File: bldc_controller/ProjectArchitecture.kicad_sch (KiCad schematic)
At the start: 0 parts

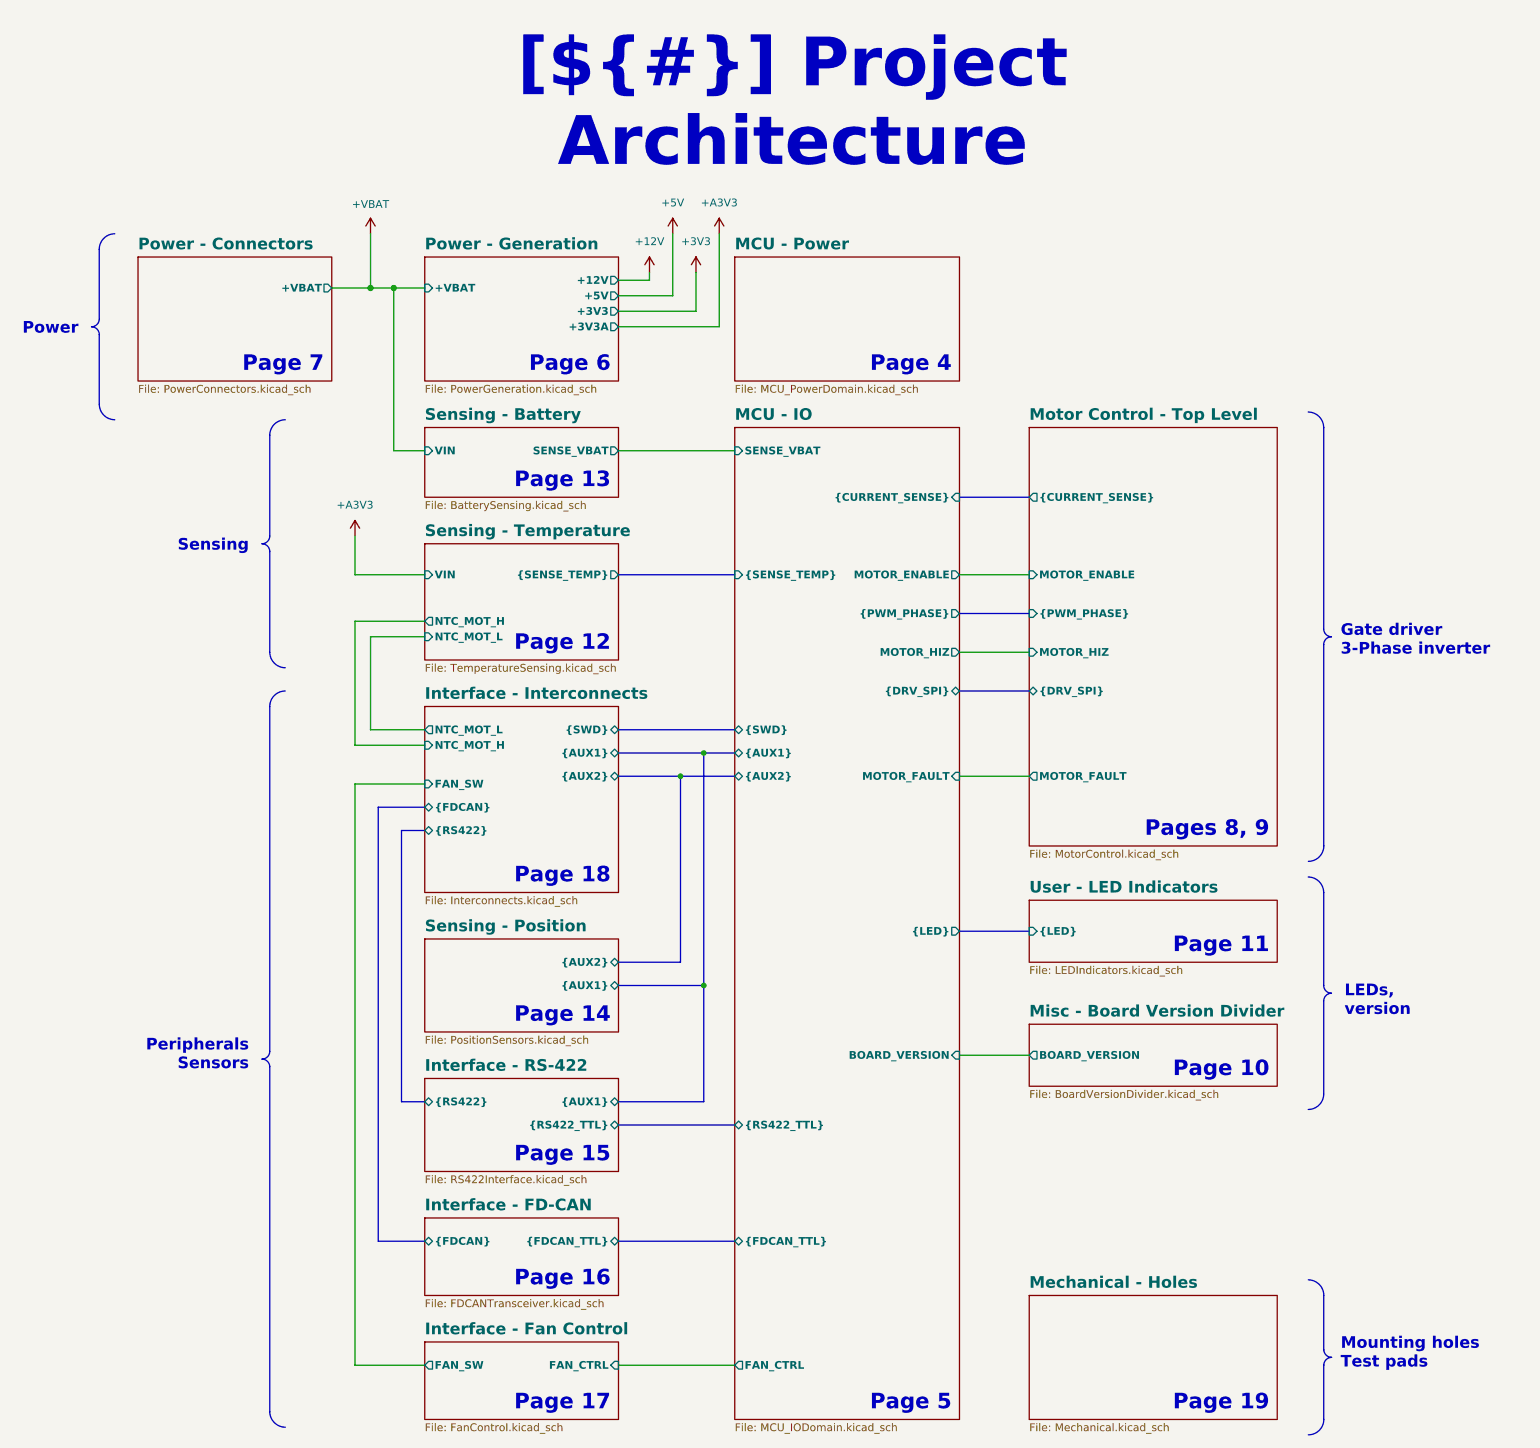
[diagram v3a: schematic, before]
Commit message: Added block diagram, currently rerouting power polygons
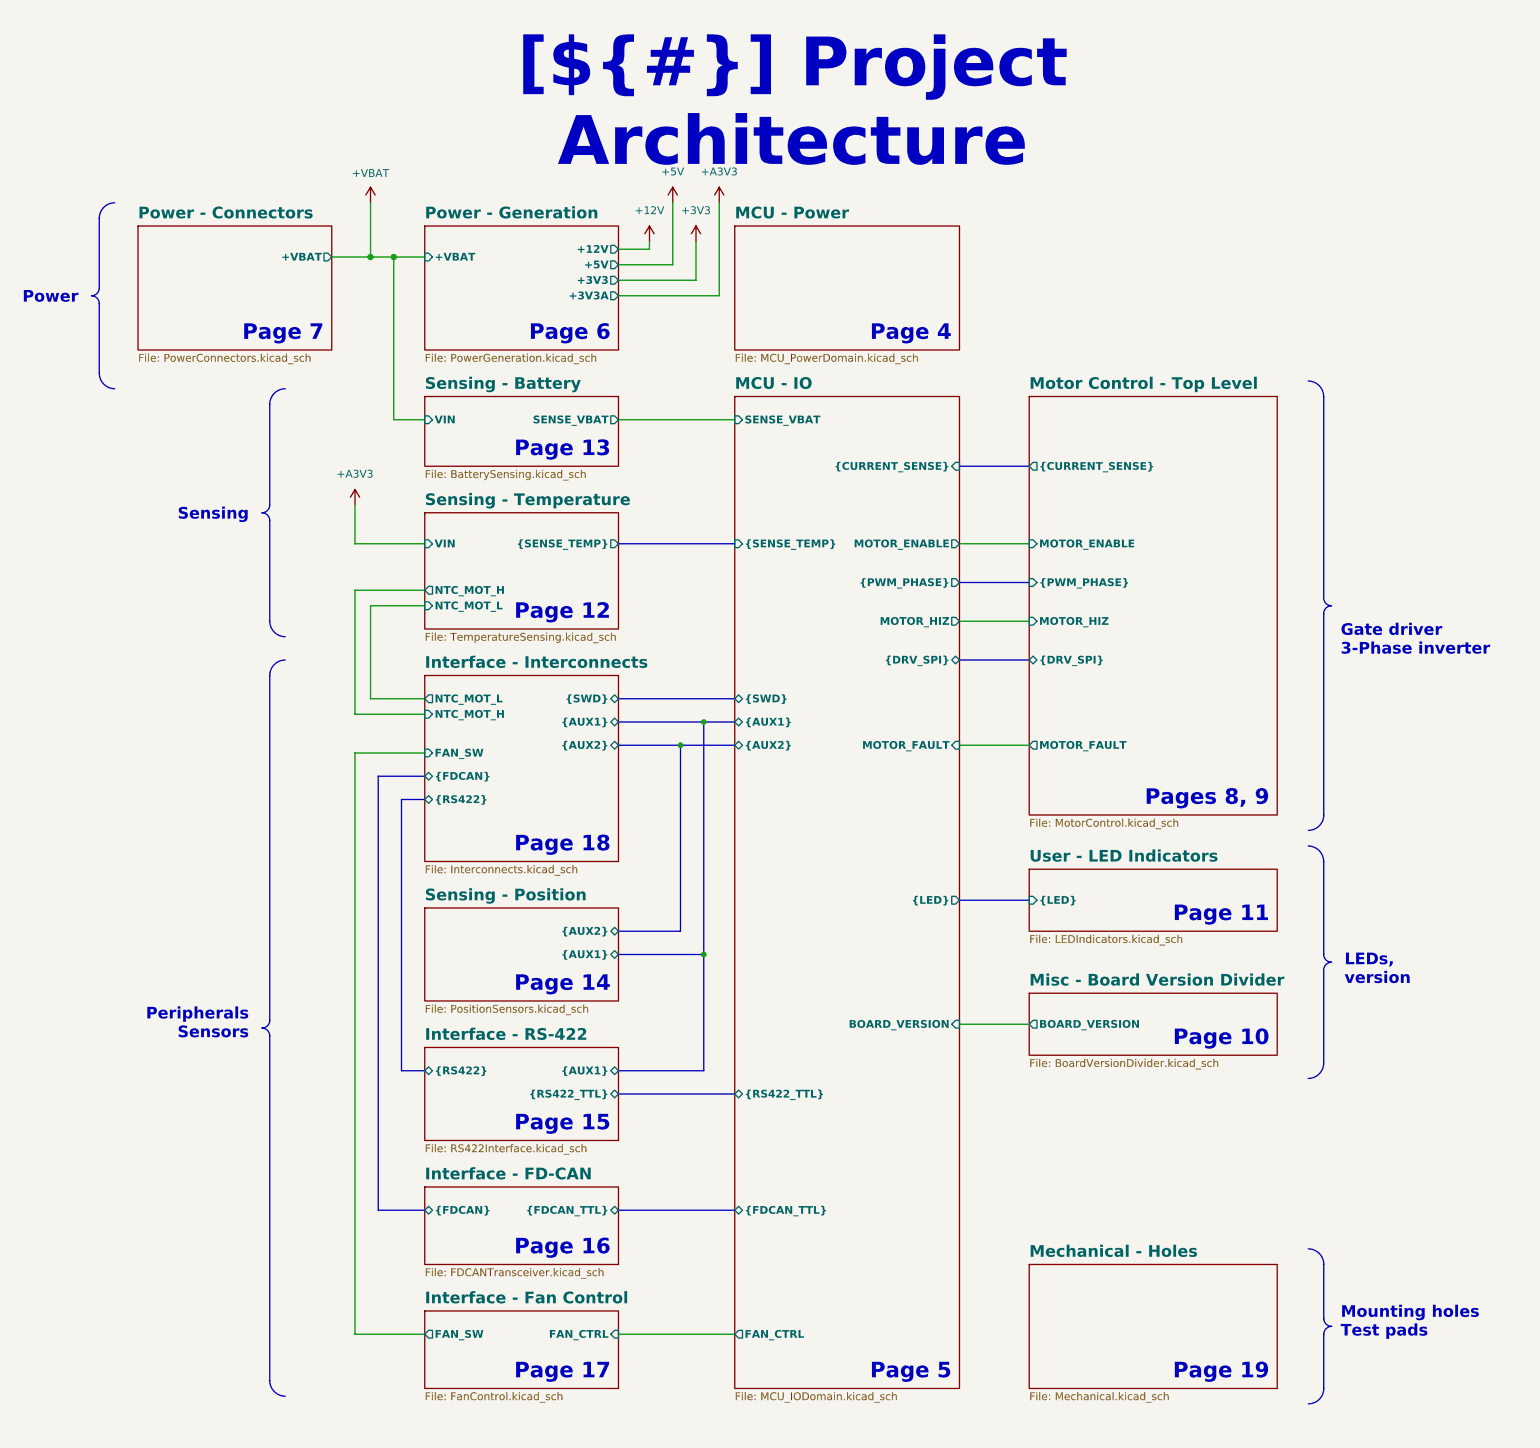
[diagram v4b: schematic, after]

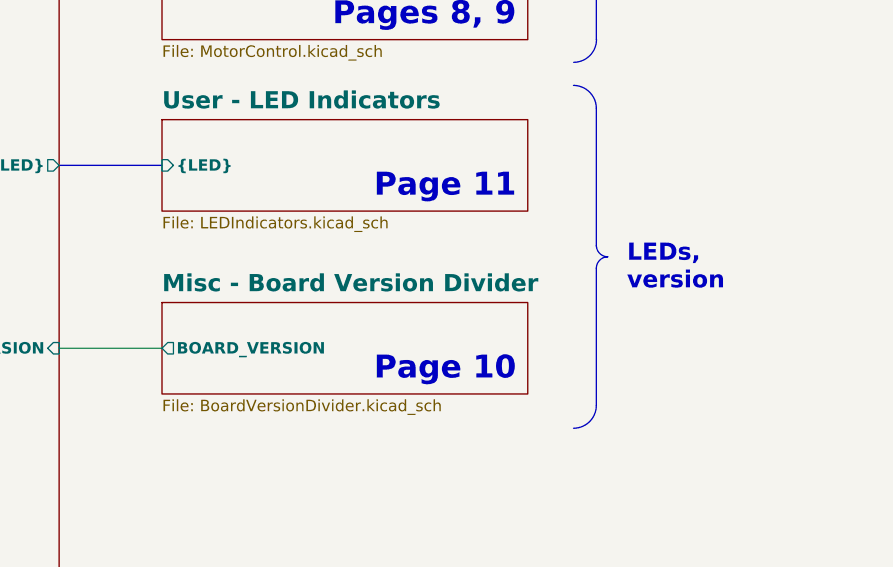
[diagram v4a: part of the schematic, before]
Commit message: finished most of routing. Need to add testpoints and clean up graphics
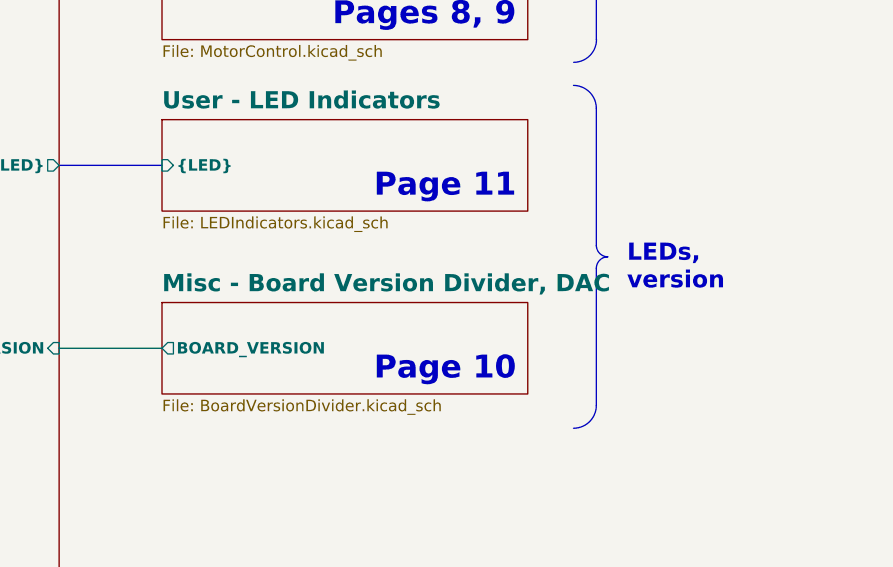
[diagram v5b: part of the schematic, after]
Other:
- sheet Misc - Board Version Divider renamed Misc - Board Version Divider, DAC
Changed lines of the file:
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@@
     (stroke (width 0.1524) (type solid))
     (fill (color 255 255 150 0.5000))
-    (property "Sheetname" "Misc - Board Version Divider" (at 248.92 171.6909 0)
+    (property "Sheetname" "Misc - Board Version Divider, DAC" (at 248.92 171.6909 0)
       (effects (font (size 1.905 1.905) bold) (justify left bottom))
     )
